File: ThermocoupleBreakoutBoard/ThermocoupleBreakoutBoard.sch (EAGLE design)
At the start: 9 parts

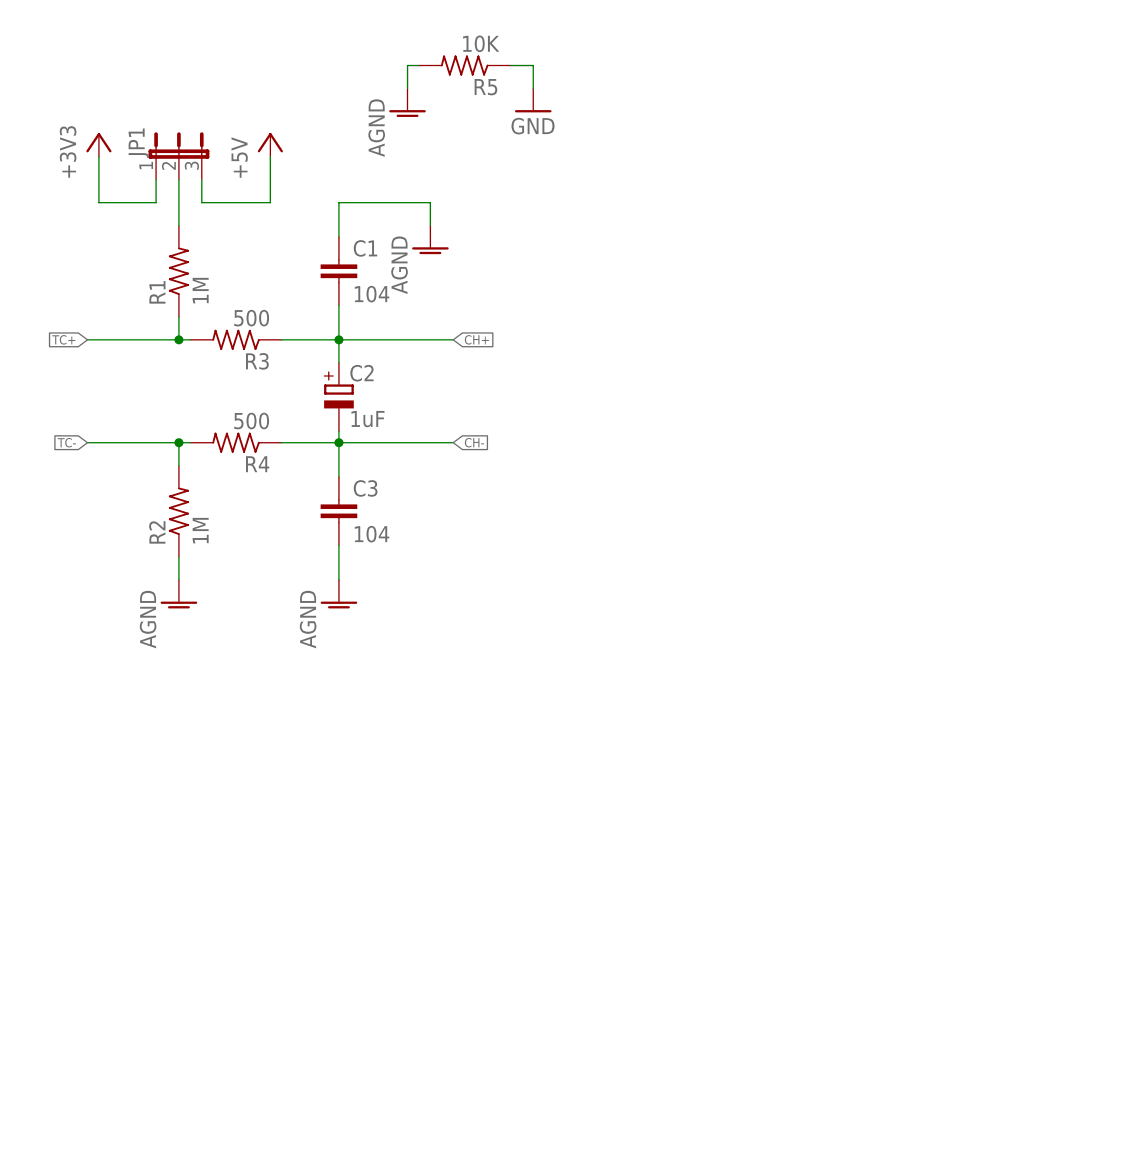
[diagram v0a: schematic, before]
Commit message: Duplicated 4-thermocouple input section
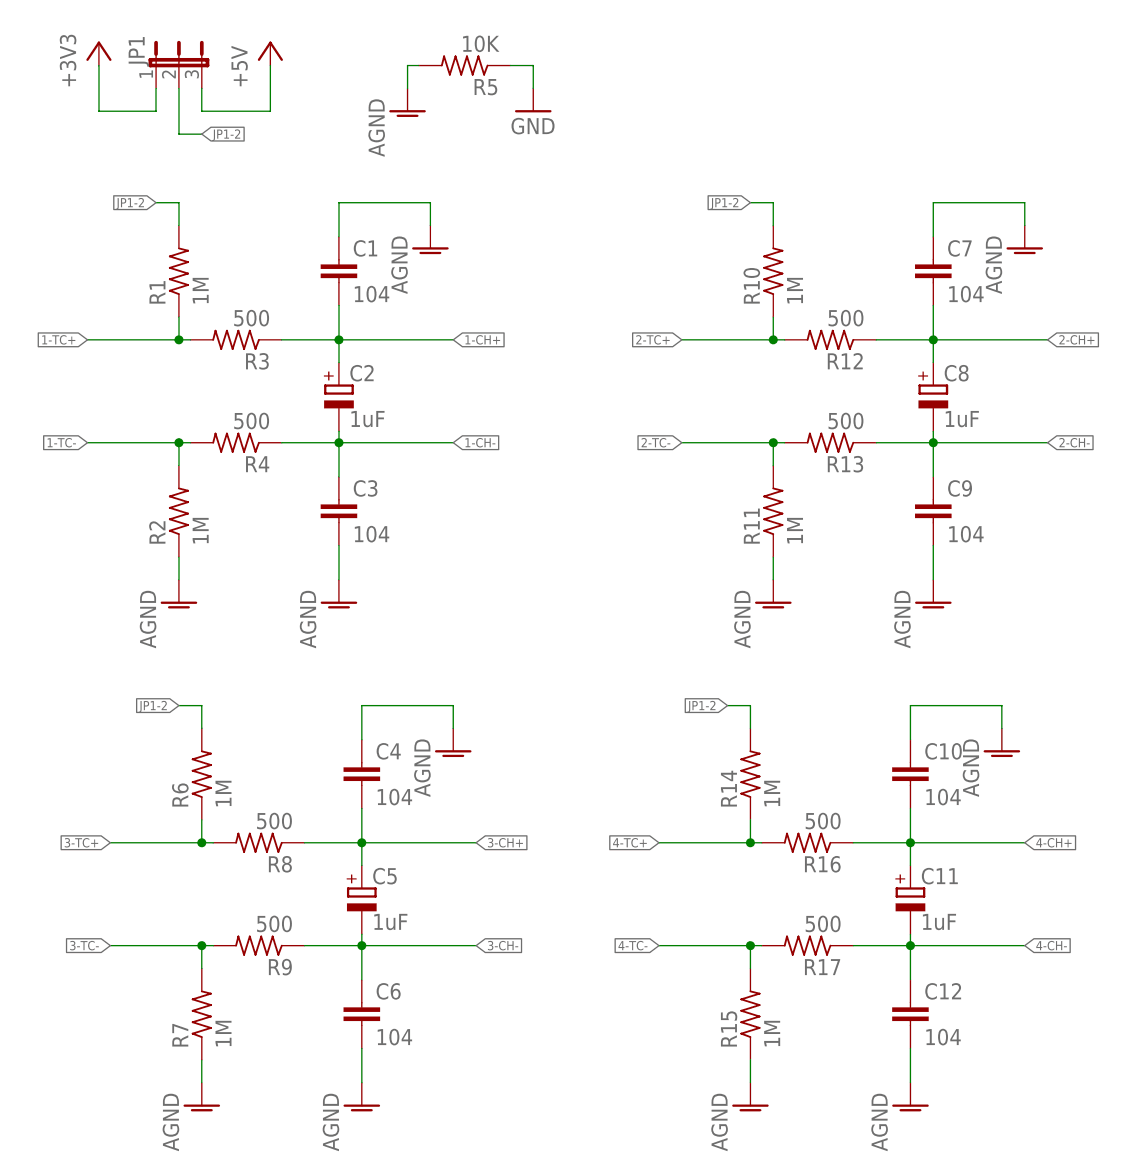
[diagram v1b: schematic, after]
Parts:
- added C10, C12, C4, C6, C7, C9: 104, rcl_vm:C-EUC1206
- added C11, C5, C8: 1uF, rcl_vm:CPOL-EUE2.5-6
- added R10, R11, R14, R15, R6, R7: 1M, rcl_vm:R-US_M1206
- added R12, R13, R16, R17, R8, R9: 500, rcl_vm:R-US_M1206
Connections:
- net CH+ renamed 1-CH+
- net CH- renamed 1-CH-
- net TC+ renamed 1-TC+
- net TC- renamed 1-TC-
- removed net N$5: JP1.2, R1.2
- new net 2-CH+: C7.2, C8.+, R12.1
- new net 2-CH-: C8.-, C9.1, R13.1
- new net 2-TC+: R10.1, R12.2
- new net 2-TC-: R11.2, R13.2
- new net 3-CH+: C4.2, C5.+, R8.1
- new net 3-CH-: C5.-, C6.1, R9.1
- new net 3-TC+: R6.1, R8.2
- new net 3-TC-: R7.2, R9.2
- new net 4-CH+: C10.2, C11.+, R16.1
- new net 4-CH-: C11.-, C12.1, R17.1
- new net 4-TC+: R14.1, R16.2
- new net 4-TC-: R15.2, R17.2
- new net JP1-2: JP1.2, R1.2, R10.2, R14.2, R6.2
- net AGND: now also C10.1, C12.2, C4.1, C6.2, C7.1, C9.2, R11.1, R15.1, R7.1
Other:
- moved on the sheet: JP1
